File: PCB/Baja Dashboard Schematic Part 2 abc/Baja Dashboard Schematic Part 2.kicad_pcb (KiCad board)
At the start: 4 copper layers, 145.5 x 72 mm, 53 parts, among them J1 Conn_01x04_Pin, J2 Conn_01x04_Pin, Q1 MMBT2222_, SW1 SW_Push, SW2 SW_Push, U1 TLC5917, U2 TLC5917, U3 TLC5917, U9 TLC555xPS

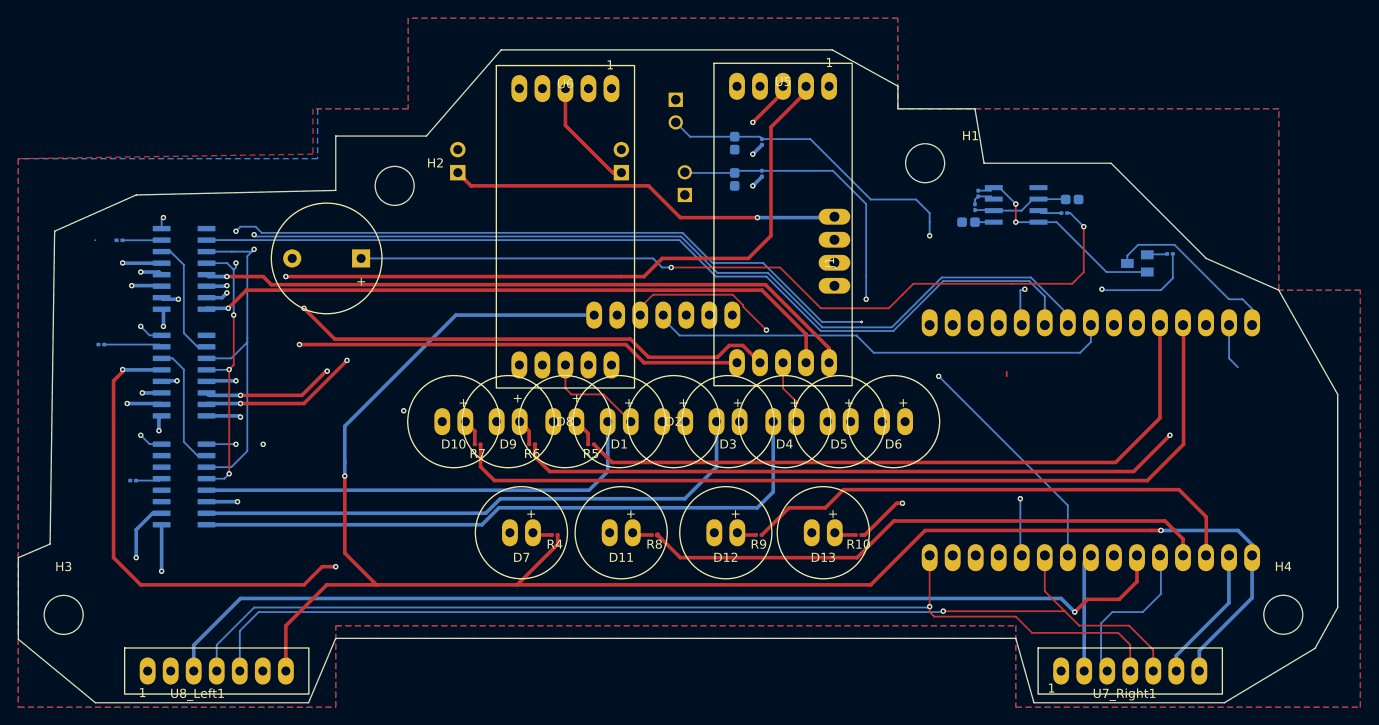
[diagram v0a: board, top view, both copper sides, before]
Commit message: New version with filleted edges
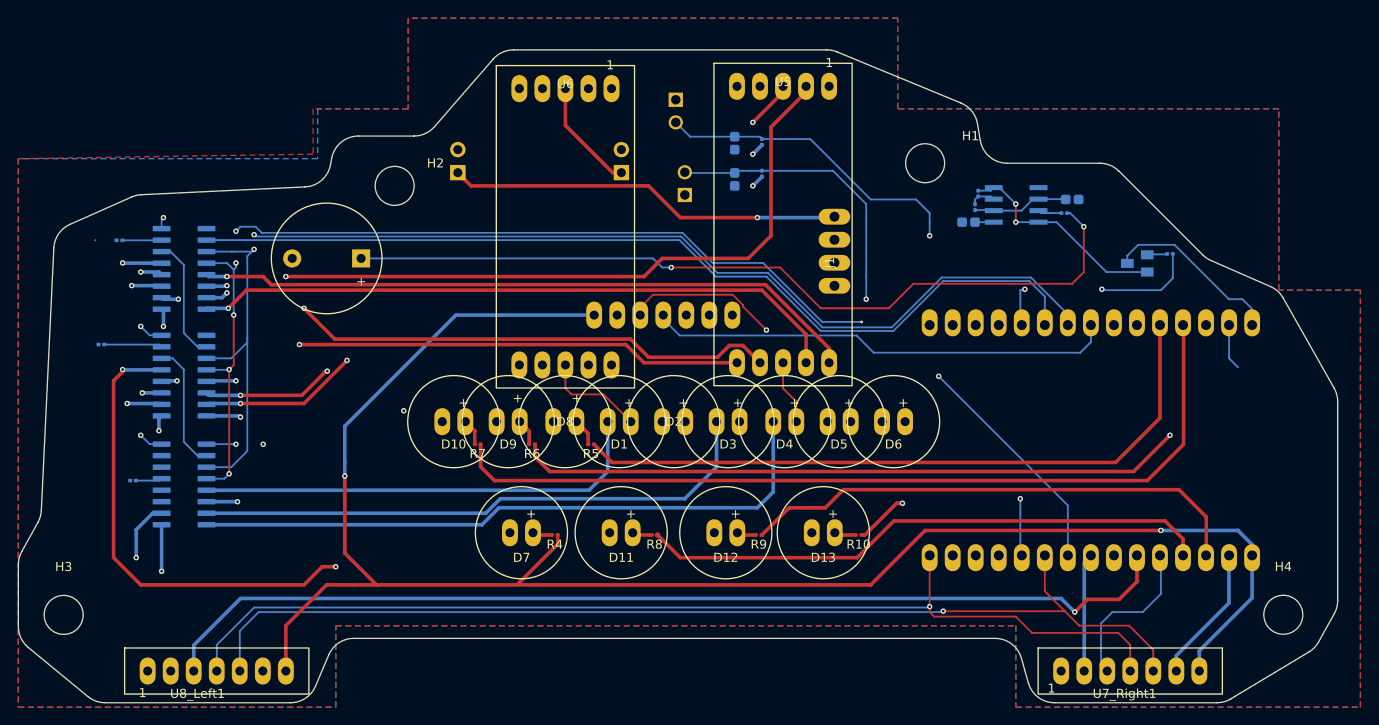
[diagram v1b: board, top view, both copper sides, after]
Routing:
- net (no net): track 0.50 -> 0.00 mm
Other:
- outline, holes or cut-outs redrawn

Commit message: Add files via upload
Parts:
- C1: value 10nF -> C1
- C2: value 10^pF -> C2
- R1: value 200 -> R1
- R11: value 300 -> R11
- R2: value 300 -> R2
- R3: value 300 -> R3
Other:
- outline, holes or cut-outs redrawn

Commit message: Add files via upload
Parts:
- R10, R4, R5, R6, R7, R8, R9: moved to B.Cu
- moved R7 0.50 mm to (130.2, 114.0)
- moved R8 0.19 mm to (149.3, 124.0)
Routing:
- net /D8LED: track 75.5 -> 76.7 mm, vias 0 -> 1
- net +3.3V: track 191.8 -> 191.5 mm, vias 2 -> 3
- net /D12LED: track 56.6 -> 56.9 mm, vias 0 -> 1
- net /D9LED: track 87.5 -> 87.3 mm, vias 1 -> 2
- net /D10LED: track 95.5 -> 95.3 mm, vias 0 -> 1
- net /D11LED: track 63.3 -> 63.1 mm, vias 0 -> 1
- net /D13LED: vias 1 -> 2

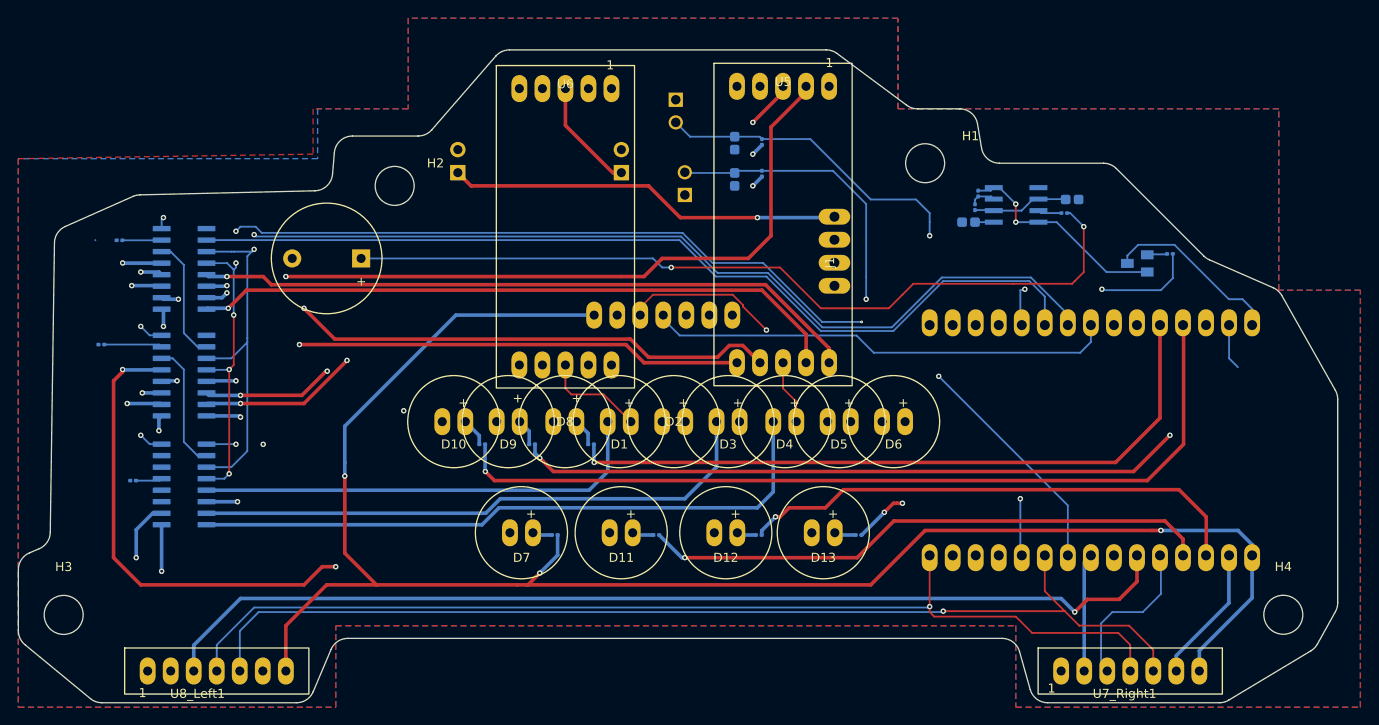
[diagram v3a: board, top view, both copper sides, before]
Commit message: Remove all Blind/Buried Vias for PCB manufacturing
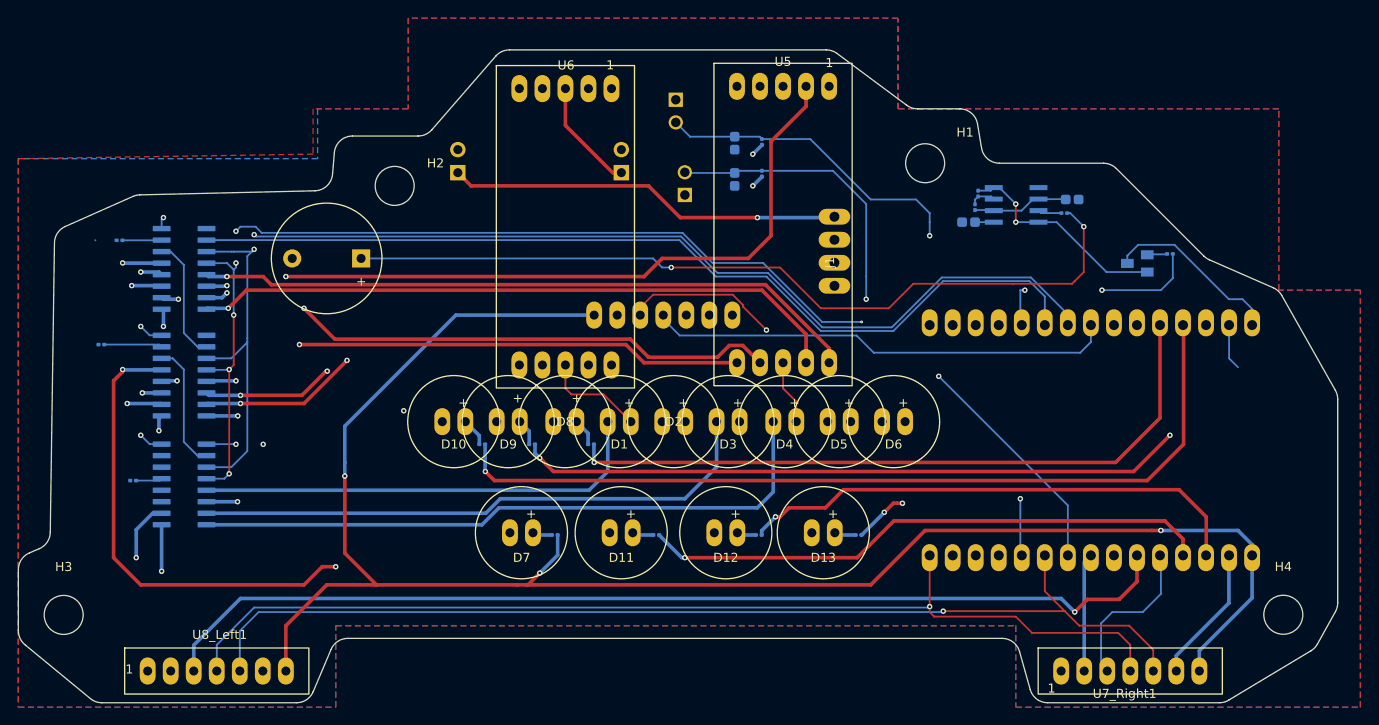
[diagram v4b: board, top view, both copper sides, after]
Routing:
- net +5V: track 65.6 -> 60.9 mm, vias 6 -> 5
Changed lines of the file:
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@@
 		(tags "mounting hole 4.3mm no annular m4")
 		(property "Reference" "H1"
-			(at 5 -3 0)
+			(at 4.4 -3.4 0)
 			(layer "F.SilkS")
 			(effects
@@
 		(at 163.33 74.52)
 		(property "Reference" "U5"
-			(at 0 -0.5 0)
+			(at 0 -2.72 0)
 			(unlocked yes)
 			(layer "F.SilkS")
@@
 		(at 139.33 74.77)
 		(property "Reference" "U6"
-			(at 0 -0.5 0)
+			(at 0.07 -2.57 0)
 			(unlocked yes)
 			(layer "F.SilkS")
@@
 		(at 93.26 139)
 		(property "Reference" "U8_Left1"
-			(at 5.5 2.5 0)
+			(at 7.94 -4 0)
 			(unlocked yes)
 			(layer "F.SilkS")
@@
 		)
 		(fp_text user "1"
-			(at -1 3 0)
+			(at -2.46 0.4 0)
 			(unlocked yes)
 			(layer "F.SilkS")
@@
 		)
 		(fp_text user "${REFERENCE}"
-			(at 0 2.5 0)
+			(at 0.54 -3.8 0)
 			(unlocked yes)
 			(layer "F.Fab")
@@
 		(tags "resistor")
 		(property "Reference" "R10"
-			(at 0 1.05 360)
+			(at 0 1.05 0)
 			(layer "B.SilkS")
 			(effects
@@
 		)
 		(property "Value" "300"
-			(at -0.845 -1.05 360)
+			(at -0.845 -1.05 0)
 			(layer "B.Fab")
 			(effects
@@
 		)
 		(fp_text user "${REFERENCE}"
-			(at 0 0.68 360)
+			(at 0 0.68 0)
 			(layer "B.Fab")
 			(effects
@@
 		(tags "resistor")
 		(property "Reference" "R5"
-			(at -0.345 -1 360)
+			(at -0.345 -1 0)
 			(layer "B.SilkS")
 			(effects
@@
 		)
 		(property "Value" "300"
-			(at 0 2.5 360)
+			(at 0 2.5 0)
 			(layer "B.Fab")
 			(effects
@@
 		)
 		(fp_text user "${REFERENCE}"
-			(at 0 0.68 360)
+			(at 0 0.68 0)
 			(layer "B.Fab")
 			(effects
@@
 		(tags "resistor")
 		(property "Reference" "R4"
-			(at 0 1.05 360)
+			(at 0 1.05 0)
 			(layer "B.SilkS")
 			(effects
@@
 		)
 		(fp_text user "${REFERENCE}"
-			(at 0 0.68 360)
+			(at 0 0.68 0)
 			(layer "B.Fab")
 			(effects
@@
 		(tags "resistor")
 		(property "Reference" "R6"
-			(at 0.155 -1 360)
+			(at 0.155 -1 0)
 			(layer "B.SilkS")
 			(effects
@@
 		)
 		(property "Value" "300"
-			(at 0.655 2.5 360)
+			(at 0.655 2.5 0)
 			(layer "B.Fab")
 			(effects
@@
 		)
 		(fp_text user "${REFERENCE}"
-			(at 0 0.68 360)
+			(at 0 0.68 0)
 			(layer "B.Fab")
 			(effects
@@
 		(tags "resistor")
 		(property "Reference" "R9"
-			(at 0 1.05 360)
+			(at 0 1.05 0)
 			(layer "B.SilkS")
 			(effects
@@
 		)
 		(property "Value" "300"
-			(at -0.845 -1.05 360)
+			(at -0.845 -1.05 0)
 			(layer "B.Fab")
 			(effects
@@
 		)
 		(fp_text user "${REFERENCE}"
-			(at 0 0.68 360)
+			(at 0 0.68 0)
 			(layer "B.Fab")
 			(effects
@@
 		(tags "resistor")
 		(property "Reference" "R7"
-			(at 0.155 -1 360)
+			(at 0.155 -1 0)
 			(layer "B.SilkS")
 			(effects
@@
 		)
 		(property "Value" "300"
-			(at 0.655 3 360)
+			(at 0.655 3 0)
 			(layer "B.Fab")
 			(effects
@@
 		)
 		(fp_text user "${REFERENCE}"
-			(at 0 0.68 360)
+			(at 0 0.68 0)
 			(layer "B.Fab")
 			(effects
@@
 		(tags "resistor")
 		(property "Reference" "R8"
-			(at 0 1.05 360)
+			(at 0 1.05 0)
 			(layer "B.SilkS")
 			(effects
@@
 		)
 		(property "Value" "300"
-			(at -0.845 -1 360)
+			(at -0.845 -1 0)
 			(layer "B.Fab")
 			(effects
@@
 		)
 		(fp_text user "${REFERENCE}"
-			(at 0 0.68 360)
+			(at 0 0.68 0)
 			(layer "B.Fab")
 			(effects
@@
 	)
 	(segment
-		(start 159.5 93.5)
-		(end 150 93.5)
+		(start 148 95.5)
+		(end 108.5 95.5)
 		(width 0.4)
 		(layer "F.Cu")
@@
 	)
 	(segment
-		(start 162 79.015)
+		(start 162 80.6)
 		(end 162 91)
 		(width 0.4)
@@
 	)
 	(segment
-		(start 148 95.5)
-		(end 145.5 95.5)
-		(width 0.4)
-		(layer "F.Cu")
-		(net 19)
-	)
-	(segment
-		(start 150 93.5)
-		(end 148 95.5)
+		(start 165.87 74.52)
+		(end 165.87 76.73)
 		(width 0.4)
 		(layer "F.Cu")
@@
 	)
 	(segment
-		(start 145.5 95.5)
-		(end 108.5 95.5)
+		(start 165.87 76.73)
+		(end 162 80.6)
 		(width 0.4)
 		(layer "F.Cu")
@@
 	)
 	(segment
-		(start 165.87 75.145)
-		(end 162 79.015)
+		(start 150 93.5)
+		(end 148 95.5)
 		(width 0.4)
 		(layer "F.Cu")
@@
 	)
 	(segment
-		(start 165.87 74.52)
-		(end 165.87 75.145)
+		(start 159.5 93.5)
+		(end 150 93.5)
 		(width 0.4)
 		(layer "F.Cu")
@@
 	)
 	(segment
-		(start 163.33 75.17)
-		(end 160 78.5)
-		(width 0.4)
-		(layer "F.Cu")
-		(net 21)
-	)
-	(segment
 		(start 145.5 84.04)
 		(end 144.54 84.04)
@@
 	)
 	(via
-		(at 92.5 113)
-		(size 0.6)
-		(drill 0.3)
-		(layers "F.Cu" "B.Cu")
-		(net 21)
-	)
-	(via
-		(at 160 78.5)
+		(at 160 82)
 		(size 0.6)
 		(drill 0.3)
@@
 	)
 	(via
-		(at 160 82)
+		(at 92.5 113)
 		(size 0.6)
 		(drill 0.3)
@@
 	)
 	(via
-		(at 103.5 111)
+		(at 103.2 110.87)
 		(size 0.6)
 		(drill 0.3)
@@
 	)
 	(segment
-		(start 103.5 111)
-		(end 122 111)
+		(start 140.4 109.1)
+		(end 142 107.5)
 		(width 0.4)
 		(layer "In1.Cu")
@@
 	)
 	(segment
-		(start 140.4 109.1)
-		(end 142 107.5)
+		(start 123.9 109.1)
+		(end 140.4 109.1)
 		(width 0.4)
 		(layer "In1.Cu")
@@
 	)
 	(segment
-		(start 142 107.5)
-		(end 142 105.38)
+		(start 142 105.38)
+		(end 141.87 105.25)
 		(width 0.4)
 		(layer "In1.Cu")
@@
 	)
 	(segment
-		(start 142 105.38)
-		(end 141.87 105.25)
+		(start 103.2 110.87)
+		(end 103.33 111)
 		(width 0.4)
 		(layer "In1.Cu")
@@
 	)
 	(segment
-		(start 123.9 109.1)
-		(end 140.4 109.1)
+		(start 142 107.5)
+		(end 142 105.38)
 		(width 0.4)
 		(layer "In1.Cu")
@@
 	)
 	(segment
-		(start 103.5 111)
-		(end 103.37 110.87)
+		(start 103.33 111)
+		(end 122 111)
 		(width 0.4)
-		(layer "B.Cu")
+		(layer "In1.Cu")
 		(net 37)
 	)
 	(segment
-		(start 103.37 110.87)
+		(start 103.2 110.87)
 		(end 99.75 110.87)
 		(width 0.4)
@@
 	)
 	(via
-		(at 198.5 96.9)
+		(at 198.5 97)
 		(size 0.6)
 		(drill 0.3)
@@
 	)
 	(via
-		(at 190 96.9)
+		(at 190 97)
 		(size 0.6)
 		(drill 0.3)
@@
 	)
 	(segment
-		(start 190.1 97)
-		(end 198.4 97)
-		(width 0.2)
-		(layer "In1.Cu")
-		(net 62)
-	)
-	(segment
-		(start 190 96.9)
-		(end 190.1 97)
+		(start 198.5 97)
+		(end 190 97)
 		(width 0.2)
 		(layer "In1.Cu")
@@
 	)
 	(segment
-		(start 198.4 97)
-		(end 198.5 96.9)
-		(width 0.2)
-		(layer "In1.Cu")
-		(net 62)
-	)
-	(segment
-		(start 198.5 96.9)
-		(end 198.6 97)
-		(width 0.2)
-		(layer "B.Cu")
-		(net 62)
-	)
-	(segment
-		(start 198.6 97)
-		(end 205 97)
+		(start 206.32 95.68)
+		(end 206.32 93)
 		(width 0.2)
 		(layer "B.Cu")
@@
 	(segment
 		(start 189.5 97)
-		(end 189.9 97)
+		(end 189.5 100.69)
 		(width 0.2)
 		(layer "B.Cu")
@@
 	)
 	(segment
-		(start 205 97)
-		(end 206.32 95.68)
+		(start 190 97)
+		(end 189.5 97)
 		(width 0.2)
 		(layer "B.Cu")
@@
 	)
 	(segment
-		(start 206.32 93)
+		(start 205 97)
 		(end 206.32 95.68)
 		(width 0.2)
@@
 	)
 	(segment
-		(start 189.9 97)
-		(end 190 96.9)
-		(width 0.2)
-		(layer "B.Cu")
-		(net 62)
-	)
-	(segment
-		(start 189.5 97)
-		(end 189.5 100.69)
+		(start 198.5 97)
+		(end 205 97)
 		(width 0.2)
 		(layer "B.Cu")
